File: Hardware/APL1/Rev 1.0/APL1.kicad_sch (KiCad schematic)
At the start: 44 parts, among them J1 6502 BUS, J2 KEYBOARD, J3 SERIAL (DTE), J4 5V DC, J5 PS/2, J6 VIDEO, SW1 POWER, U1 74LS04, U10 ATmega1284-P, U2 6502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

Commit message: Change KBDCLRB to KBDCLR (active high)
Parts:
- added R9: 10k, Resistor_THT:R_Axial_DIN0207_L6.3mm_D2.5mm_P10.16mm_Horizontal, symbol Device:R
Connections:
- net GND: now also R9.1
- net KBDCLRB renamed KBDCLR
- net KBDCLR: now also R9.2
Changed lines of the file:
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@@
 	)
 	(junction
+		(at 369.57 120.65)
+		(diameter 0)
+		(color 0 0 0 0)
+	)
+	(junction
 		(at 276.86 134.62)
 		(diameter 0)
@@
 	(wire
 		(pts
+			(xy 369.57 120.65) (xy 369.57 123.19)
+		)
+		(stroke
+			(width 0)
+			(type default)
+		)
+	)
+	(wire
+		(pts
 			(xy 154.94 185.42) (xy 154.94 186.69)
 		)
@@
 	(wire
 		(pts
-			(xy 347.98 120.65) (xy 350.52 120.65)
+			(xy 347.98 120.65) (xy 369.57 120.65)
 		)
 		(stroke
@@
 	(wire
 		(pts
+			(xy 369.57 130.81) (xy 369.57 133.35)
+		)
+		(stroke
+			(width 0)
+			(type default)
+		)
+	)
+	(wire
+		(pts
 			(xy 62.23 146.05) (xy 64.77 146.05)
 		)
@@
 	(wire
 		(pts
+			(xy 369.57 120.65) (xy 375.92 120.65)
+		)
+		(stroke
+			(width 0)
+			(type default)
+		)
+	)
+	(wire
+		(pts
 			(xy 266.7 64.77) (xy 266.7 68.58)
 		)
@@
 		)
 	)
-	(global_label "KBDCLRB"
+	(global_label "KBDCLR"
 		(shape input)
-		(at 350.52 120.65 0)
+		(at 375.92 120.65 0)
 		(fields_autoplaced yes)
 		(effects
@@
 		)
 		(property "Intersheetrefs" "${INTERSHEET_REFS}"
-			(at 362.1533 120.65 0)
+			(at 386.2833 120.65 0)
 			(hide yes)
 			(show_name no)
@@
 		)
 	)
-	(global_label "KBDCLRB"
+	(global_label "KBDCLR"
 		(shape output)
 		(at 228.6 52.07 0)
@@
 		)
 		(property "Intersheetrefs" "${INTERSHEET_REFS}"
-			(at 240.2333 52.07 0)
+			(at 238.9633 52.07 0)
 			(hide yes)
 			(show_name no)
@@
 	)
 	(symbol
+		(lib_id "Device:R")
+		(at 369.57 127 180)
+		(unit 1)
+		(body_style 1)
+		(exclude_from_sim no)
+		(in_bom yes)
+		(on_board yes)
+		(in_pos_files yes)
+		(dnp no)
+		(property "Reference" "R9"
+			(at 373.634 125.984 0)
+			(show_name no)
+			(do_not_autoplace no)
+			(effects
+				(font
+					(size 1.27 1.27)
+				)
+			)
+		)
+		(property "Value" "10k"
+			(at 373.634 128.524 0)
+			(show_name no)
+			(do_not_autoplace no)
+			(effects
+				(font
+					(size 1.27 1.27)
+				)
+			)
+		)
+		(property "Footprint" "Resistor_THT:R_Axial_DIN0207_L6.3mm_D2.5mm_P10.16mm_Horizontal"
+			(at 371.348 127 90)
+			(hide yes)
+			(show_name no)
+			(do_not_autoplace no)
+			(effects
+				(font
+					(size 1.27 1.27)
+				)
+			)
+		)
+		(property "Datasheet" ""
+			(at 369.57 127 0)
+			(hide yes)
+			(show_name no)
+			(do_not_autoplace no)
+			(effects
+				(font
+					(size 1.27 1.27)
+				)
+			)
+		)
+		(property "Description" "Resistor"
+			(at 369.57 127 0)
+			(hide yes)
+			(show_name no)
+			(do_not_autoplace no)
+			(effects
+				(font
+					(size 1.27 1.27)
+				)
+			)
+		)
+		(pin "2"
+		)
+		(pin "1"
+		)
+		(instances
+			(project "APL1"
+				(path "/458d8e11-1191-4776-ab30-0ba4a61904aa"
+					(reference "R9")
+					(unit 1)
+				)
+			)
+		)
+	)
+	(symbol
 		(lib_id "power:GND")
 		(at 375.92 160.02 0)
@@
 					(unit 1)
 				)
+			)
+		)
+	)
+	(symbol
+		(lib_id "power:GND")
+		(at 369.57 133.35 0)
+		(unit 1)
+		(body_style 1)
+		(exclude_from_sim no)
+		(in_bom yes)
+		(on_board yes)
+		(in_pos_files yes)
+		(dnp no)
+		(fields_autoplaced yes)
+		(property "Reference" "#PWR024"
+			(at 369.57 139.7 0)
+			(hide yes)
+			(show_name no)
+			(do_not_autoplace no)
+			(effects
+				(font
+					(size 1.27 1.27)
+				)
+			)
+		)
+		(property "Value" "GND"
+			(at 369.57 138.43 0)
+			(hide yes)
+			(show_name no)
+			(do_not_autoplace no)
+			(effects
+				(font
+					(size 1.27 1.27)
+				)
+			)
+		)
+		(property "Footprint" ""
+			(at 369.57 133.35 0)
+			(hide yes)
+			(show_name no)
+			(do_not_autoplace no)
+			(effects
+				(font
+					(size 1.27 1.27)
+				)
+			)
+		)
+		(property "Datasheet" ""
+			(at 369.57 133.35 0)
+			(hide yes)
+			(show_name no)
+			(do_not_autoplace no)
+			(effects
+				(font
+					(size 1.27 1.27)
+				)
+			)
+		)
+		(property "Description" "Power symbol creates a global label with name \"GND\" , ground"
+			(at 369.57 133.35 0)
+			(hide yes)
+			(show_name no)
+			(do_not_autoplace no)
+			(effects
+				(font
+					(size 1.27 1.27)
+				)
+			)
+		)
+		(pin "1"
+		)
+		(instances
+			(project "APL1"
+				(path "/458d8e11-1191-4776-ab30-0ba4a61904aa"
+					(reference "#PWR024")
+					(unit 1)
+				)

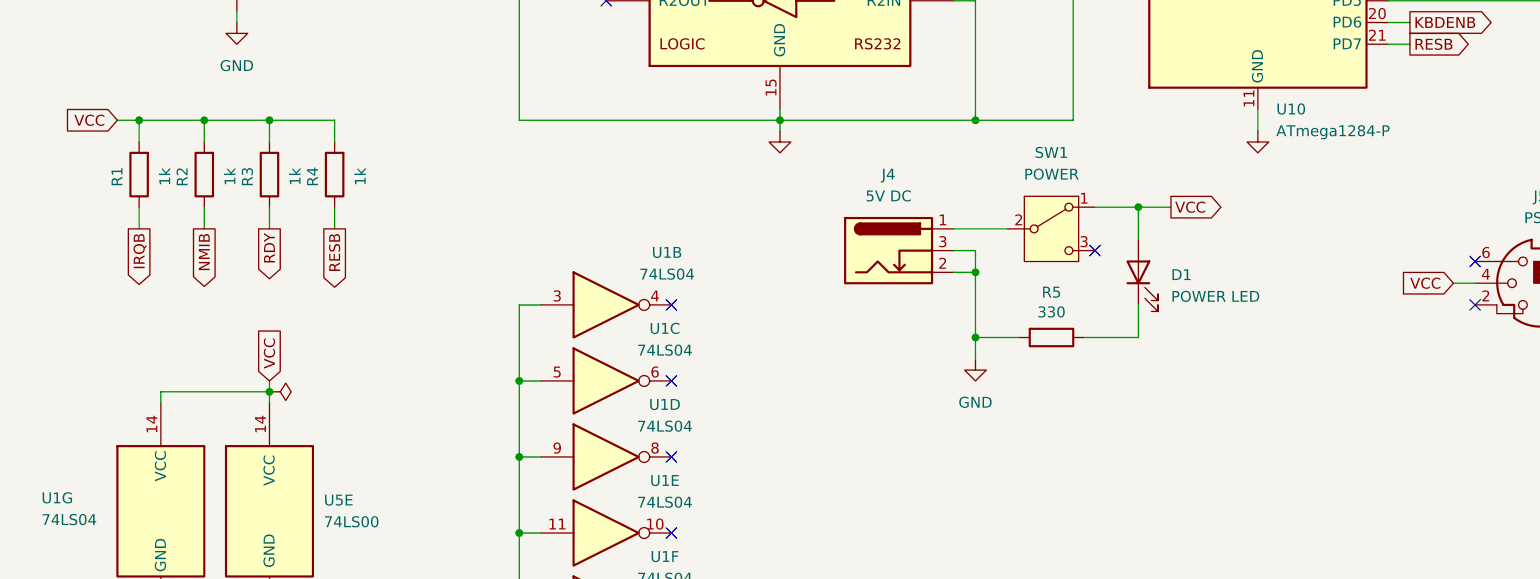
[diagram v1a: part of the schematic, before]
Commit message: Fix silkscreen and add bulk capacitance
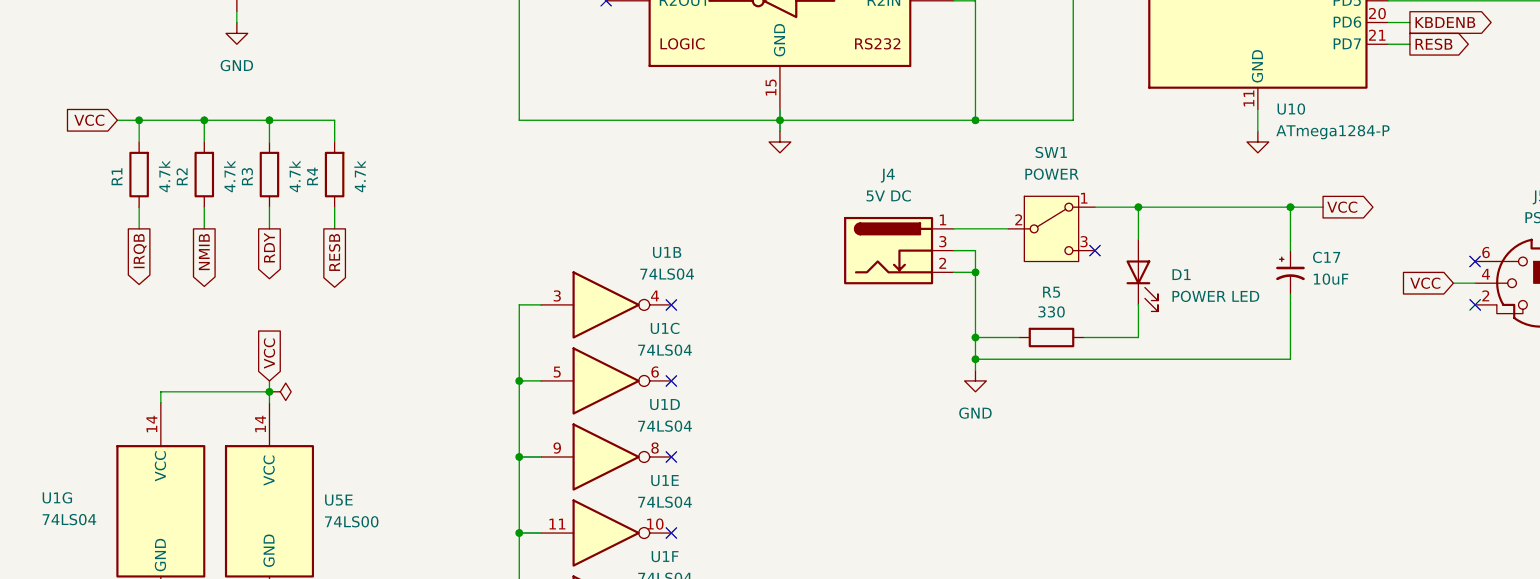
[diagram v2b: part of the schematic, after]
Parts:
- added C17: 10uF, Capacitor_THT:CP_Radial_D4.0mm_P1.50mm, symbol Device:C_Polarized_Small_US
- R1, R2, R3, R4: value 1k -> 4.7k
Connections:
- net GND: now also C17.2
- net VCC: now also C17.1
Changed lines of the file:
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@@
 	)
 	(junction
+		(at 299.72 162.56)
+		(diameter 0)
+		(color 0 0 0 0)
+	)
+	(junction
 		(at 314.96 58.42)
 		(diameter 0)
@@
 	)
 	(junction
+		(at 336.55 144.78)
+		(diameter 0)
+		(color 0 0 0 0)
+	)
+	(junction
 		(at 173.99 193.04)
 		(diameter 0)
@@
 	)
 	(junction
+		(at 318.77 144.78)
+		(diameter 0)
+		(color 0 0 0 0)
+	)
+	(junction
 		(at 306.07 40.64)
 		(diameter 0)
@@
 	)
 	(junction
-		(at 318.77 144.78)
-		(diameter 0)
-		(color 0 0 0 0)
-	)
-	(junction
 		(at 217.17 166.37)
 		(diameter 0)
@@
 	(wire
 		(pts
-			(xy 318.77 144.78) (xy 322.58 144.78)
+			(xy 318.77 144.78) (xy 336.55 144.78)
 		)
 		(stroke
@@
 	(wire
 		(pts
+			(xy 336.55 144.78) (xy 340.36 144.78)
+		)
+		(stroke
+			(width 0)
+			(type default)
+		)
+	)
+	(wire
+		(pts
 			(xy 153.67 128.27) (xy 156.21 128.27)
 		)
@@
 	(wire
 		(pts
+			(xy 336.55 162.56) (xy 299.72 162.56)
+		)
+		(stroke
+			(width 0)
+			(type default)
+		)
+	)
+	(wire
+		(pts
 			(xy 226.06 99.06) (xy 228.6 99.06)
 		)
@@
 	(wire
 		(pts
+			(xy 336.55 144.78) (xy 336.55 149.86)
+		)
+		(stroke
+			(width 0)
+			(type default)
+		)
+	)
+	(wire
+		(pts
 			(xy 276.86 133.35) (xy 276.86 134.62)
 		)
@@
 	(wire
 		(pts
+			(xy 299.72 163.83) (xy 299.72 162.56)
+		)
+		(stroke
+			(width 0)
+			(type default)
+		)
+	)
+	(wire
+		(pts
 			(xy 29.21 151.13) (xy 31.75 151.13)
 		)
@@
 	(wire
 		(pts
+			(xy 336.55 154.94) (xy 336.55 162.56)
+		)
+		(stroke
+			(width 0)
+			(type default)
+		)
+	)
+	(wire
+		(pts
 			(xy 367.03 90.17) (xy 369.57 90.17)
 		)
@@
 	(global_label "VCC"
 		(shape output)
-		(at 322.58 144.78 0)
+		(at 340.36 144.78 0)
 		(effects
 			(font
@@
 		)
 		(property "Intersheetrefs" "${INTERSHEET_REFS}"
-			(at 322.58 144.78 0)
+			(at 340.36 144.78 0)
 			(hide yes)
 			(show_name no)
@@
 	(symbol
 		(lib_id "power:GND")
-		(at 299.72 162.56 0)
+		(at 299.72 163.83 0)
 		(unit 1)
 		(body_style 1)
@@
 		(fields_autoplaced yes)
 		(property "Reference" "#PWR019"
-			(at 299.72 168.91 0)
+			(at 299.72 170.18 0)
 			(hide yes)
 			(show_name no)
@@
 		)
 		(property "Value" "GND"
-			(at 299.72 167.64 0)
+			(at 299.72 168.91 0)
 			(show_name no)
 			(do_not_autoplace no)
@@
 		)
 		(property "Footprint" ""
-			(at 299.72 162.56 0)
+			(at 299.72 163.83 0)
 			(hide yes)
 			(show_name no)
@@
 		)
 		(property "Datasheet" ""
-			(at 299.72 162.56 0)
+			(at 299.72 163.83 0)
 			(hide yes)
 			(show_name no)
@@
 		)
 		(property "Description" "Power symbol creates a global label with name \"GND\" , ground"
-			(at 299.72 162.56 0)
+			(at 299.72 163.83 0)
 			(hide yes)
 			(show_name no)
@@
 	)
 	(symbol
+		(lib_id "Device:C_Polarized_Small_US")
+		(at 336.55 152.4 0)
+		(unit 1)
+		(body_style 1)
+		(exclude_from_sim no)
+		(in_bom yes)
+		(on_board yes)
+		(in_pos_files yes)
+		(dnp no)
+		(fields_autoplaced yes)
+		(property "Reference" "C17"
+			(at 339.09 150.6981 0)
+			(show_name no)
+			(do_not_autoplace no)
+			(effects
+				(font
+					(size 1.27 1.27)
+				)
+				(justify left)
+			)
+		)
+		(property "Value" "10uF"
+			(at 339.09 153.2381 0)
+			(show_name no)
+			(do_not_autoplace no)
+			(effects
+				(font
+					(size 1.27 1.27)
+				)
+				(justify left)
+			)
+		)
+		(property "Footprint" "Capacitor_THT:CP_Radial_D4.0mm_P1.50mm"
+			(at 336.55 152.4 0)
+			(hide yes)
+			(show_name no)
+			(do_not_autoplace no)
+			(effects
+				(font
+					(size 1.27 1.27)
+				)
+			)
+		)
+		(property "Datasheet" ""
+			(at 336.55 152.4 0)
+			(hide yes)
+			(show_name no)
+			(do_not_autoplace no)
+			(effects
+				(font
+					(size 1.27 1.27)
+				)
+			)
+		)
+		(property "Description" "Polarized capacitor, small US symbol"
+			(at 336.55 152.4 0)
+			(hide yes)
+			(show_name no)
+			(do_not_autoplace no)
+			(effects
+				(font
+					(size 1.27 1.27)
+				)
+			)
+		)
+		(pin "1"
+		)
+		(pin "2"
+		)
+		(instances
+			(project "APL1"
+				(path "/458d8e11-1191-4776-ab30-0ba4a61904aa"
+					(reference "C17")
+					(unit 1)
+				)
+			)
+		)
+	)
+	(symbol
 		(lib_id "6502 Parts:KMDGX-6S-BS")
 		(at 365.76 153.67 0)
@@
 			)
 		)
-		(property "Value" "1k"
+		(property "Value" "4.7k"
 			(at 212.598 141.224 90)
 			(show_name no)
@@
 			)
 		)
-		(property "Value" "1k"
+		(property "Value" "4.7k"
 			(at 220.218 141.224 90)
 			(show_name no)
@@
 			)
 		)
-		(property "Value" "1k"
+		(property "Value" "4.7k"
 			(at 227.838 141.224 90)
 			(show_name no)
@@
 			)
 		)
-		(property "Value" "1k"
+		(property "Value" "4.7k"
 			(at 204.978 141.224 90)
 			(show_name no)
